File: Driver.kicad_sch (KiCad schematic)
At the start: 36 parts

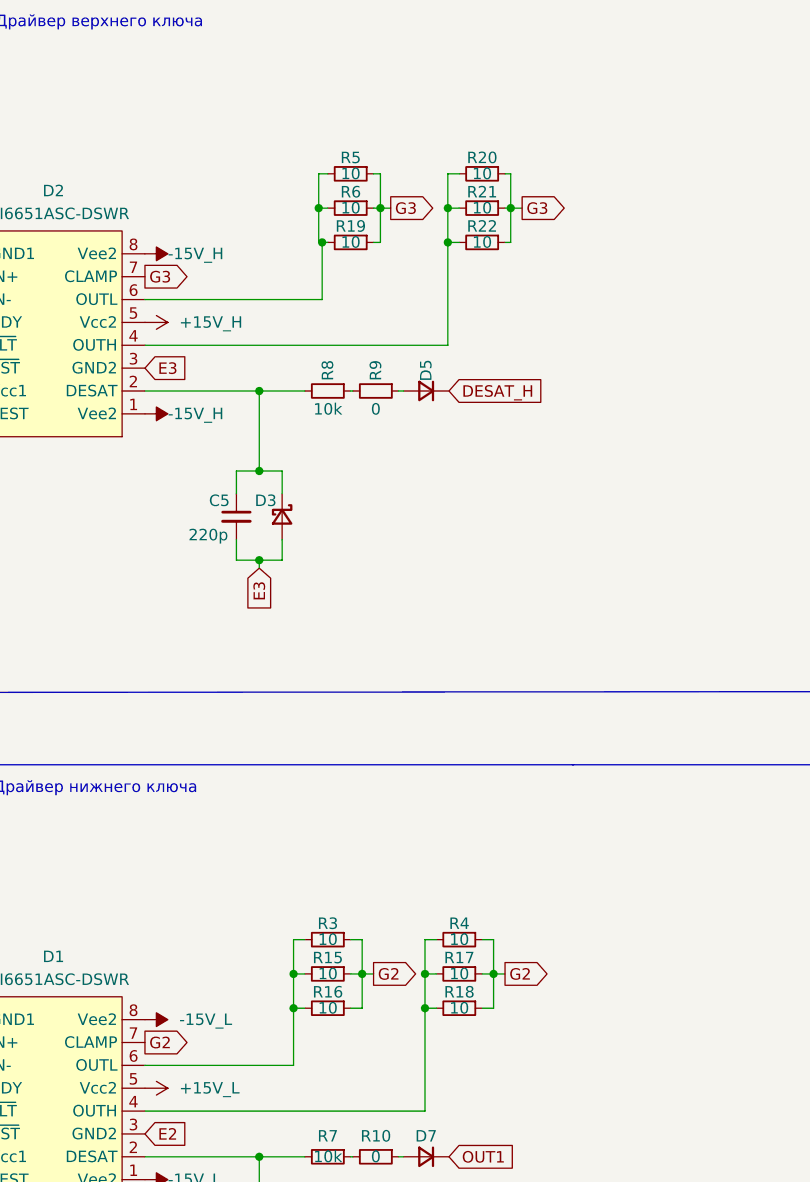
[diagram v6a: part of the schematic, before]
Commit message: Изменения: изменил BOM, сделал заказ
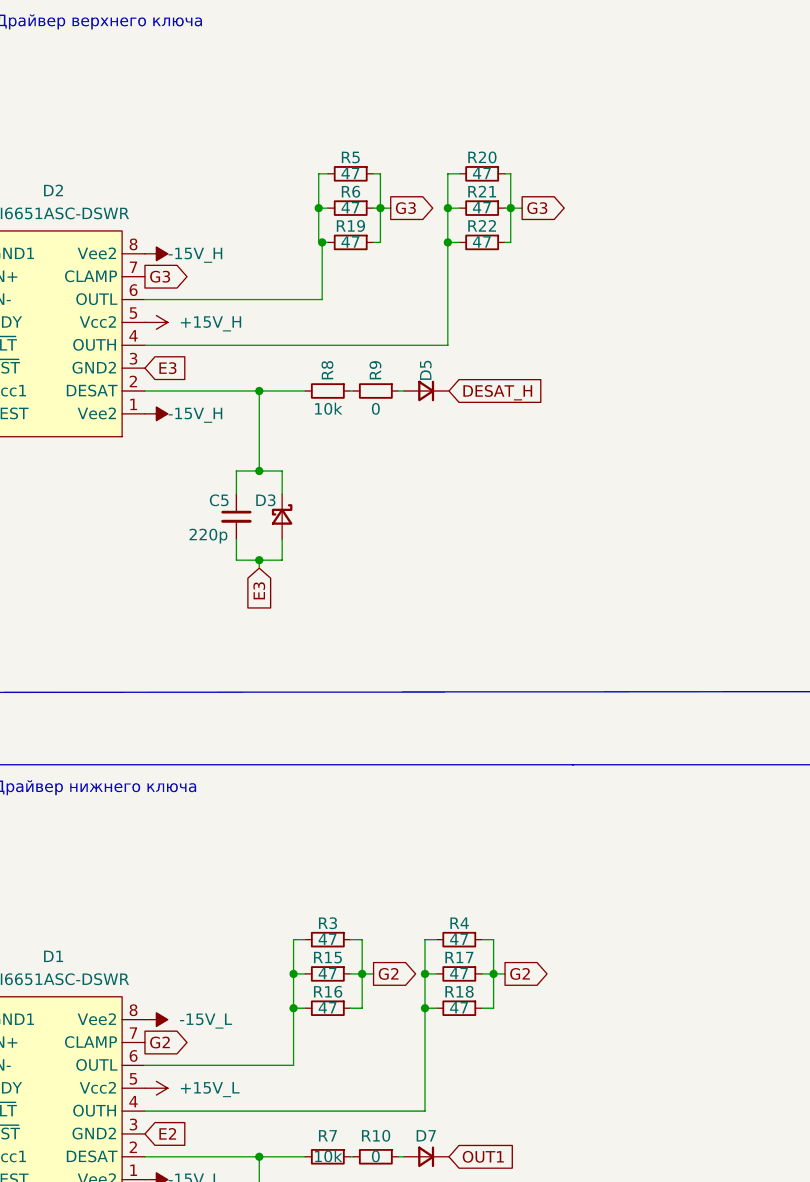
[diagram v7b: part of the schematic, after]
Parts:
- R15, R16, R17, R18, R19, R20, R21, R22, R3, R4, R5, R6: value 10 -> 47
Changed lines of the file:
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@@
 			)
 		)
-		(property "Value" "10"
+		(property "Value" "47"
 			(at 122.555 50.165 90)
 			(effects
@@
 			)
 		)
-		(property "Value" "10"
+		(property "Value" "47"
 			(at 105.41 135.255 90)
 			(effects
@@
 			)
 		)
-		(property "Value" "10"
+		(property "Value" "47"
 			(at 107.95 46.355 90)
 			(effects
@@
 			)
 		)
-		(property "Value" "10"
+		(property "Value" "47"
 			(at 122.555 46.355 90)
 			(effects
@@
 			)
 		)
-		(property "Value" "10"
+		(property "Value" "47"
 			(at 120.015 127.635 90)
 			(effects
@@
 			)
 		)
-		(property "Value" "10"
+		(property "Value" "47"
 			(at 122.555 42.545 90)
 			(effects
@@
 			)
 		)
-		(property "Value" "10"
+		(property "Value" "47"
 			(at 120.015 135.255 90)
 			(effects
@@
 			)
 		)
-		(property "Value" "10"
+		(property "Value" "47"
 			(at 105.41 131.445 90)
 			(effects
@@
 			)
 		)
-		(property "Value" "10"
+		(property "Value" "47"
 			(at 107.95 42.545 90)
 			(effects
@@
 			)
 		)
-		(property "Value" "10"
+		(property "Value" "47"
 			(at 120.015 131.445 90)
 			(effects
@@
 			)
 		)
-		(property "Value" "10"
+		(property "Value" "47"
 			(at 105.41 127.635 90)
 			(effects
@@
 			)
 		)
-		(property "Value" "10"
+		(property "Value" "47"
 			(at 107.95 50.165 90)
 			(effects

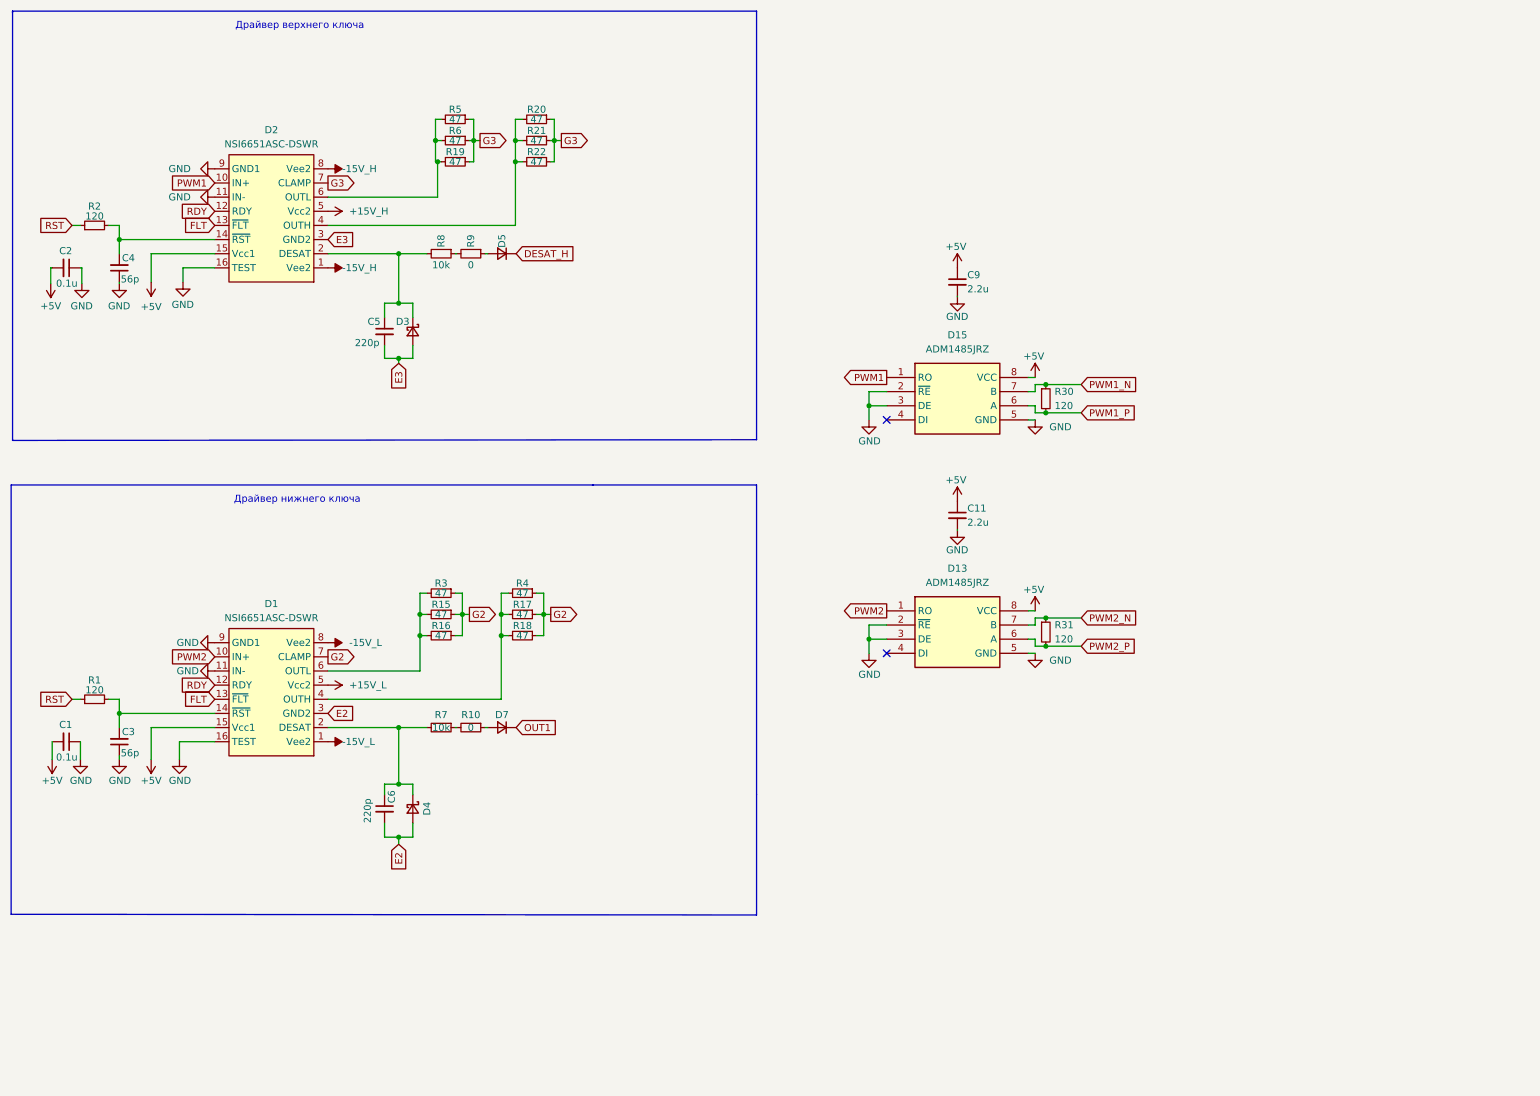
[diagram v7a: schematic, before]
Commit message: VER2.1: внес все исправления для заказа в Китае
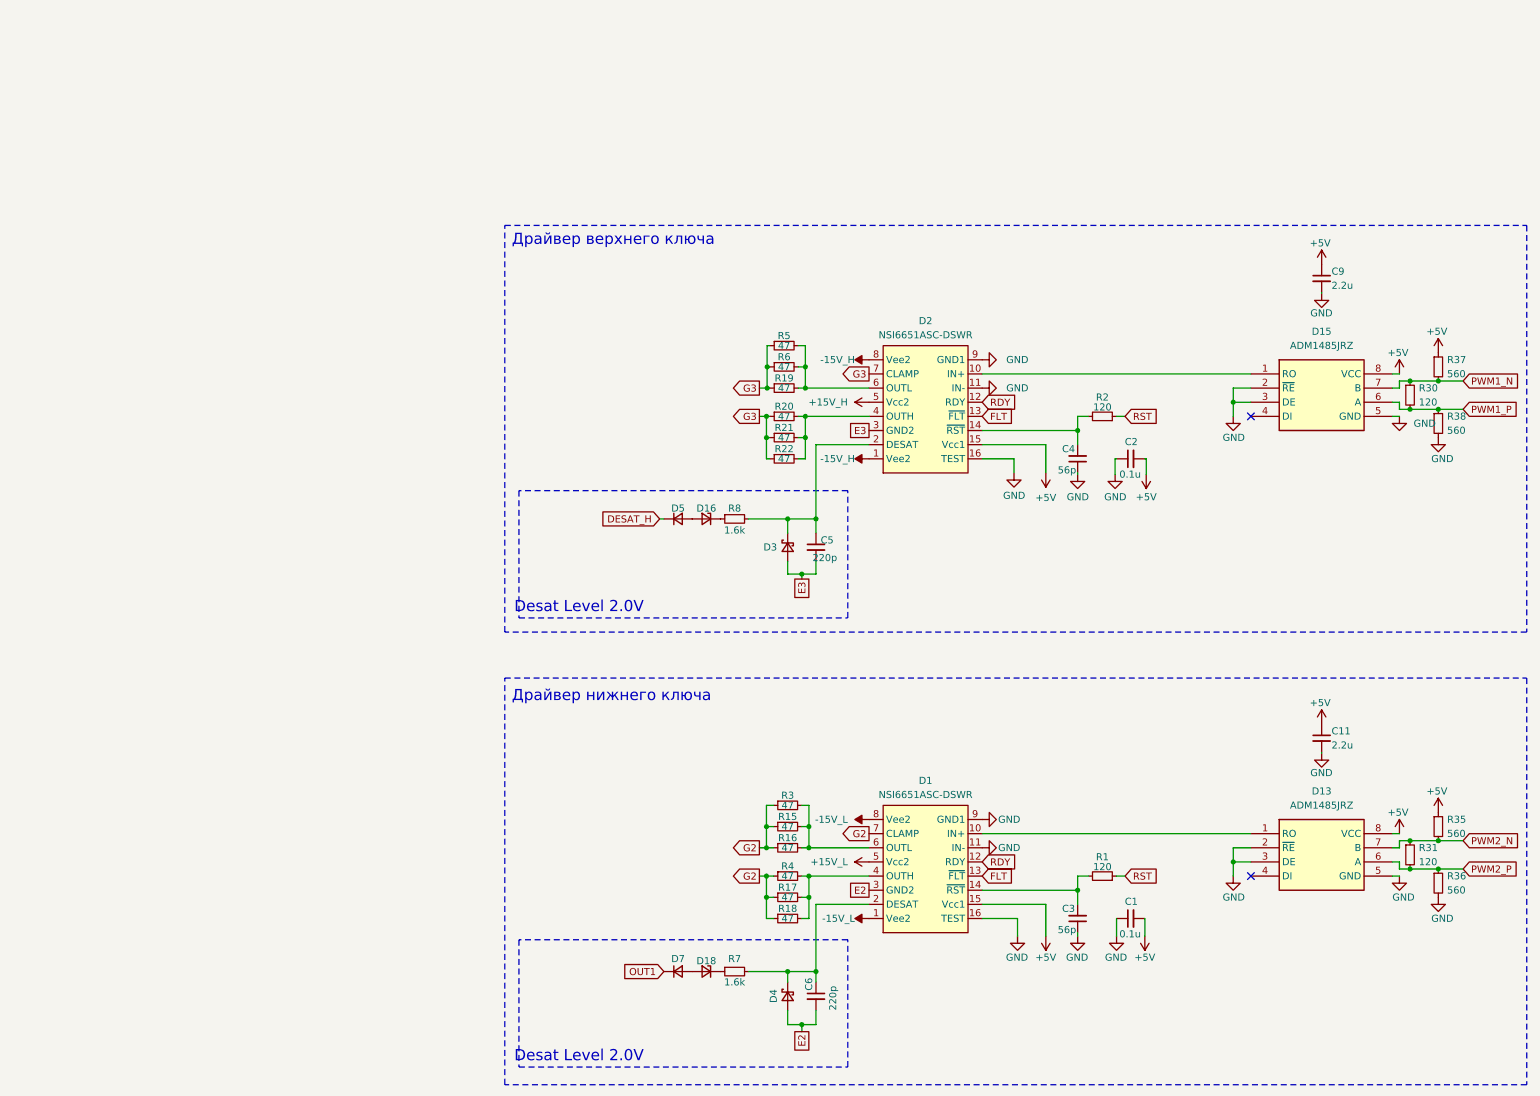
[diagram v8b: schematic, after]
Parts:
- removed R10, R9: 0, Resistor_SMD:R_0805_2012Metric_Pad1.20x1.40mm_HandSolder, symbol Device:R_Small
- added D16, D18: 1SMB5919B, Diode_SMD:D_SOD-323_HandSoldering, symbol Device:D_Zener_Small
- added R35, R36, R37, R38: 560, Resistor_SMD:R_0805_2012Metric_Pad1.20x1.40mm_HandSolder, symbol Device:R_Small
- R7, R8: value 10k -> 1.6k
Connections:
- net +5V: now also R35.1, R37.1
- net GND: now also R36.2, R38.2
- net PWM1_N: now also R37.2
- net PWM1_P: now also R38.1
- net PWM2_N: now also R35.2
- net PWM2_P: now also R36.1
- net at D5.2 (A): now also D16.2 (A)
- net at R8.1: now also D16.1 (K)
- net at D7.2 (A): now also D18.2 (A)
- net at R7.1: now also D18.1 (K)
- net PWM1: no longer names the net of D15.1 (RO), D2.10 (IN+)
- net PWM2: no longer names the net of D1.10 (IN+), D13.1 (RO)
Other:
- note added: "Desat Level 2.0V"
- moved on the sheet: C1, C11, C2, C3, C4, C5, C6, C9, D1, D13, D15, D2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
